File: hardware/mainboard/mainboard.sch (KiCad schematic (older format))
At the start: 7 parts, among them J1 2309407-1, J3 Conn_01x02_Male

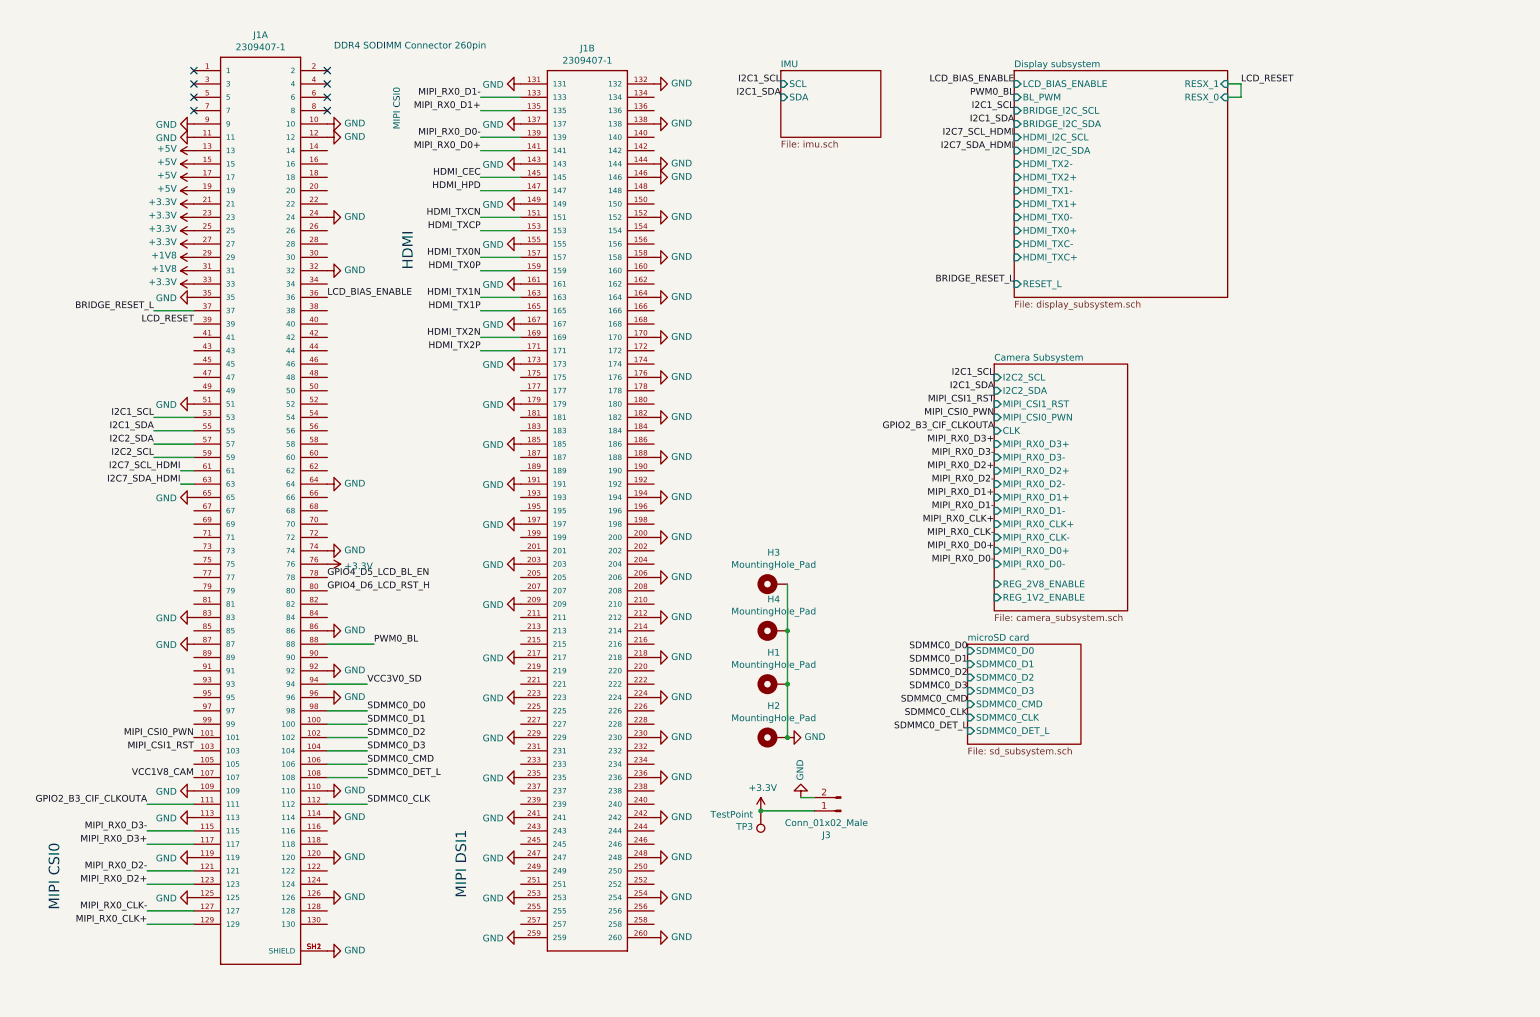
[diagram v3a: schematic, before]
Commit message: finish basic schematic, need to decide audio situation
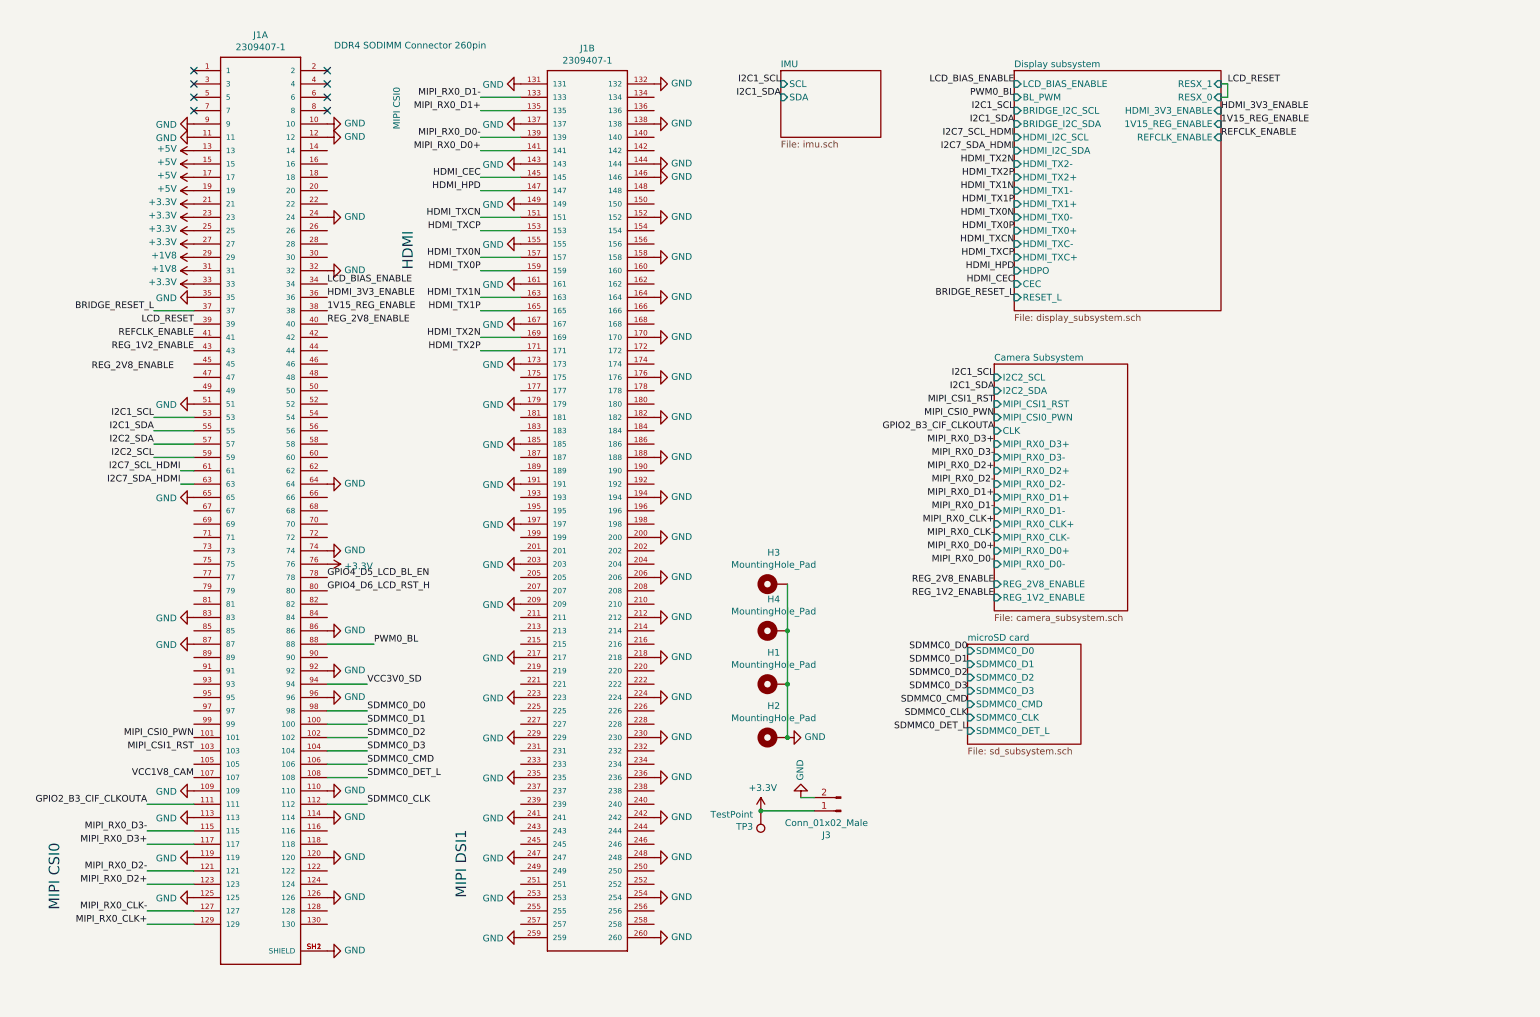
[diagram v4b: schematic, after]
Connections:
- net LCD_BIAS_ENABLE: now also J1.34; no longer J1.36
- net 1V15_REG_ENABLE: now reaches J1.38
- net REG_2V8_ENABLE: now reaches J1.40
- net REFCLK_ENABLE: now reaches J1.41
- net REG_1V2_ENABLE: now reaches J1.43
- new net HDMI_3V3_ENABLE: J1.36
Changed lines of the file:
@@
 F3 "SDA" I L 6150 1100 50
-$EndSheet
-$Sheet
-S 7900 900  1600 1700
-U 5FF71A49
-F0 "Display subsystem" 50
-F1 "display_subsystem.sch" 50
-F2 "LCD_BIAS_ENABLE" I L 7900 1000 50
-F3 "RESET_L" I L 7900 2500 50
-F4 "HDMI_TXC+" I L 7900 2300 50
-F5 "HDMI_TXC-" I L 7900 2200 50
-F6 "HDMI_TX0+" I L 7900 2100 50
-F7 "HDMI_TX0-" I L 7900 2000 50
-F8 "HDMI_TX1+" I L 7900 1900 50
-F9 "HDMI_TX1-" I L 7900 1800 50
-F10 "HDMI_TX2+" I L 7900 1700 50
-F11 "HDMI_TX2-" I L 7900 1600 50
-F12 "HDMI_I2C_SDA" I L 7900 1500 50
-F13 "HDMI_I2C_SCL" I L 7900 1400 50
-F14 "BRIDGE_I2C_SDA" I L 7900 1300 50
-F15 "BRIDGE_I2C_SCL" I L 7900 1200 50
-F16 "BL_PWM" I L 7900 1100 50
-F17 "RESX_1" I R 9500 1000 50
-F18 "RESX_0" I R 9500 1100 50
 $EndSheet
 Text Label 7750 3500 2    50   ~ 0
@@
 Text Label 7900 1000 2    50   ~ 0
 LCD_BIAS_ENABLE
-Text Label 2750 2600 0    50   ~ 0
+Text Label 2750 2500 0    50   ~ 0
 LCD_BIAS_ENABLE
 Text Label 7900 1100 2    50   ~ 0
@@
 Text Label 7900 1500 2    50   ~ 0
 I2C7_SDA_HDMI
-Text Label 7900 2500 2    50   ~ 0
+Text Label 7900 2600 2    50   ~ 0
 BRIDGE_RESET_L
 Text Label 1450 2700 2    50   ~ 0
@@
 Text Label 1750 2800 2    50   ~ 0
 LCD_RESET
-Text Label 9600 1000 0    50   ~ 0
+Text Label 9500 1000 0    50   ~ 0
 LCD_RESET
+$Sheet
+S 7900 900  1550 1800
+U 5FF71A49
+F0 "Display subsystem" 50
+F1 "display_subsystem.sch" 50
+F2 "LCD_BIAS_ENABLE" I L 7900 1000 50
+F3 "RESET_L" I L 7900 2600 50
+F4 "HDMI_TXC+" I L 7900 2300 50
+F5 "HDMI_TXC-" I L 7900 2200 50
+F6 "HDMI_TX0+" I L 7900 2100 50
+F7 "HDMI_TX0-" I L 7900 2000 50
+F8 "HDMI_TX1+" I L 7900 1900 50
+F9 "HDMI_TX1-" I L 7900 1800 50
+F10 "HDMI_TX2+" I L 7900 1700 50
+F11 "HDMI_TX2-" I L 7900 1600 50
+F12 "HDMI_I2C_SDA" I L 7900 1500 50
+F13 "HDMI_I2C_SCL" I L 7900 1400 50
+F14 "BRIDGE_I2C_SDA" I L 7900 1300 50
+F15 "BRIDGE_I2C_SCL" I L 7900 1200 50
+F16 "BL_PWM" I L 7900 1100 50
+F17 "RESX_1" I R 9450 1000 50
+F18 "RESX_0" I R 9450 1100 50
+F19 "CEC" I L 7900 2500 50
+F20 "HDPO" I L 7900 2400 50
+F21 "HDMI_3V3_ENABLE" I R 9450 1200 50
+F22 "1V15_REG_ENABLE" I R 9450 1300 50
+F23 "REFCLK_ENABLE" I R 9450 1400 50
+$EndSheet
+Text Label 7900 2300 2    50   ~ 0
+HDMI_TXCP
+Text Label 7900 2200 2    50   ~ 0
+HDMI_TXCN
+Text Label 7900 2100 2    50   ~ 0
+HDMI_TX0P
+Text Label 7900 2000 2    50   ~ 0
+HDMI_TX0N
+Text Label 7900 1900 2    50   ~ 0
+HDMI_TX1P
+Text Label 7900 1800 2    50   ~ 0
+HDMI_TX1N
+Text Label 7900 1700 2    50   ~ 0
+HDMI_TX2P
+Text Label 7900 1600 2    50   ~ 0
+HDMI_TX2N
 Wire Wire Line
-	9500 1000 9600 1000
+	9450 1000 9500 1000
 Wire Wire Line
-	9500 1100 9600 1100
+	9500 1000 9500 1100
 Wire Wire Line
-	9600 1100 9600 1000
+	9500 1100 9450 1100
+Text Label 7900 2400 2    50   ~ 0
+HDMI_HPD
+Text Label 7900 2500 2    50   ~ 0
+HDMI_CEC
+Text Label 9450 1200 0    50   ~ 0
+HDMI_3V3_ENABLE
+Text Label 9450 1300 0    50   ~ 0
+1V15_REG_ENABLE
+Text Label 9450 1400 0    50   ~ 0
+REFCLK_ENABLE
+Text Label 2750 2600 0    50   ~ 0
+HDMI_3V3_ENABLE
+Text Label 1750 2900 2    50   ~ 0
+REFCLK_ENABLE
+Text Label 2750 2700 0    50   ~ 0
+1V15_REG_ENABLE
+Text Label 7750 4850 2    50   ~ 0
+REG_1V2_ENABLE
+Text Label 1750 3000 2    50   ~ 0
+REG_1V2_ENABLE
+Text Label 7750 4750 2    50   ~ 0
+REG_2V8_ENABLE
+Text Label 1600 3150 2    50   ~ 0
+REG_2V8_ENABLE
+Text Label 2750 2800 0    50   ~ 0
+REG_2V8_ENABLE
 $EndSCHEMATC

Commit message: cleanup, audio pll, decide board layout
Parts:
- added FID? (x5): Fiducial, symbol Mechanical:Fiducial
- added J?: Conn_01x02_Male, Connector_PinHeader_2.54mm:PinHeader_1x02_P2.54mm_Vertical, symbol Connector:Conn_01x02_Male
- added TP? (x2): TestPoint, symbol Connector:TestPoint
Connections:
- net I2C1_SCL: now also TP?.1
- net I2C1_SDA: now also TP?.1
- net 1V8_REG_ENABLE: now reaches J1.42
- net UART2DBG_TX: now reaches J1.52
- net UART2DBG_TX: now also J?.1 (Pin_1)
- net UART2DBG_RX: now reaches J1.54
- net UART2DBG_RX: now also J?.2 (Pin_2)
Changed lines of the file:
@@
 $Descr A4 11693 8268
 encoding utf-8
-Sheet 1 7
+Sheet 1 8
 Title ""
 Date ""
@@
 Wire Wire Line
 	1450 3800 1750 3800
-Text Label 6150 1000 2    50   ~ 0
+Text Label 6000 1000 2    50   ~ 0
 I2C1_SCL
-Text Label 6150 1100 2    50   ~ 0
+Text Label 6000 1100 2    50   ~ 0
 I2C1_SDA
 $Comp
@@
 F0 "microSD card" 50
 F1 "sd_subsystem.sch" 50
-F2 "SDMMC0_D2" I L 7550 5450 50
-F3 "SDMMC0_D3" I L 7550 5550 50
-F4 "SDMMC0_CMD" I L 7550 5650 50
-F5 "SDMMC0_CLK" I L 7550 5750 50
-F6 "SDMMC0_D0" I L 7550 5250 50
-F7 "SDMMC0_D1" I L 7550 5350 50
-F8 "SDMMC0_DET_L" I L 7550 5850 50
+F2 "SDMMC0_D2" I L 7550 5700 50
+F3 "SDMMC0_D3" I L 7550 5600 50
+F4 "SDMMC0_CMD" I L 7550 5500 50
+F5 "SDMMC0_CLK" I L 7550 5400 50
+F6 "SDMMC0_D0" I L 7550 5900 50
+F7 "SDMMC0_D1" I L 7550 5800 50
+F8 "SDMMC0_DET_L" I L 7550 5300 50
 $EndSheet
-Text Label 7550 5250 2    50   ~ 0
+Text Label 7550 5900 2    50   ~ 0
 SDMMC0_D0
-Text Label 7550 5350 2    50   ~ 0
+Text Label 7550 5800 2    50   ~ 0
 SDMMC0_D1
-Text Label 7550 5550 2    50   ~ 0
+Text Label 7550 5600 2    50   ~ 0
 SDMMC0_D3
-Text Label 7550 5650 2    50   ~ 0
+Text Label 7550 5500 2    50   ~ 0
 SDMMC0_CMD
-Text Label 7550 5850 2    50   ~ 0
+Text Label 7550 5300 2    50   ~ 0
 SDMMC0_DET_L
-Text Label 7550 5750 2    50   ~ 0
+Text Label 7550 5400 2    50   ~ 0
 SDMMC0_CLK
-Text Label 7550 5450 2    50   ~ 0
+Text Label 7550 5700 2    50   ~ 0
 SDMMC0_D2
 Text Label 7750 3200 2    50   ~ 0
@@
 F22 "1V15_REG_ENABLE" I R 9450 1300 50
 F23 "REFCLK_ENABLE" I R 9450 1400 50
+F24 "BRIDGE_1V8_REG_ENABLE" I R 9450 1600 50
 $EndSheet
 Text Label 7900 2300 2    50   ~ 0
@@
 Text Label 7750 4750 2    50   ~ 0
 REG_2V8_ENABLE
-Text Label 1600 3150 2    50   ~ 0
-REG_2V8_ENABLE
 Text Label 2750 2800 0    50   ~ 0
 REG_2V8_ENABLE
+$Comp
+L Mechanical:Fiducial FID?
+U 1 1 5FEFD4AC
+P 6050 3150
+F 0 "FID?" H 6135 3196 50  0000 L CNN
+F 1 "Fiducial" H 6135 3105 50  0000 L CNN
+F 2 "" H 6050 3150 50  0001 C CNN
+F 3 "~" H 6050 3150 50  0001 C CNN
+	1    6050 3150
+	1    0    0    -1
+$EndComp
+$Comp
+L Mechanical:Fiducial FID?
+U 1 1 5FEFDC53
+P 6050 3450
+F 0 "FID?" H 6135 3496 50  0000 L CNN
+F 1 "Fiducial" H 6135 3405 50  0000 L CNN
+F 2 "" H 6050 3450 50  0001 C CNN
+F 3 "~" H 6050 3450 50  0001 C CNN
+	1    6050 3450
+	1    0    0    -1
+$EndComp
+$Comp
+L Mechanical:Fiducial FID?
+U 1 1 5FEFEBAF
+P 6050 3750
+F 0 "FID?" H 6135 3796 50  0000 L CNN
+F 1 "Fiducial" H 6135 3705 50  0000 L CNN
+F 2 "" H 6050 3750 50  0001 C CNN
+F 3 "~" H 6050 3750 50  0001 C CNN
+	1    6050 3750
+	1    0    0    -1
+$EndComp
+$Comp
+L Mechanical:Fiducial FID?
+U 1 1 5FEFFA9D
+P 6050 4050
+F 0 "FID?" H 6135 4096 50  0000 L CNN
+F 1 "Fiducial" H 6135 4005 50  0000 L CNN
+F 2 "" H 6050 4050 50  0001 C CNN
+F 3 "~" H 6050 4050 50  0001 C CNN
+	1    6050 4050
+	1    0    0    -1
+$EndComp
+$Comp
+L Mechanical:Fiducial FID?
+U 1 1 5FF00982
+P 6050 4350
+F 0 "FID?" H 6135 4396 50  0000 L CNN
+F 1 "Fiducial" H 6135 4305 50  0000 L CNN
+F 2 "" H 6050 4350 50  0001 C CNN
+F 3 "~" H 6050 4350 50  0001 C CNN
+	1    6050 4350
+	1    0    0    -1
+$EndComp
+Wire Wire Line
+	6000 1000 6150 1000
+Wire Wire Line
+	6000 1100 6150 1100
+$Comp
+L Connector:TestPoint TP?
+U 1 1 5FF30886
+P 6000 1100
+AR Path="/5FF71A49/5FF30886" Ref="TP?"  Part="1"
+AR Path="/5FF30886" Ref="TP?"  Part="1"
+F 0 "TP?" V 5954 1288 50  0001 L CNN
+F 1 "TestPoint" V 6045 1288 50  0001 L CNN
+F 2 "" H 6200 1100 50  0001 C CNN
+F 3 "~" H 6200 1100 50  0001 C CNN
+	1    6000 1100
+	-1   0    0    1
+$EndComp
+$Comp
+L Connector:TestPoint TP?
+U 1 1 5FF31F81
+P 6000 1000
+AR Path="/5FF71A49/5FF31F81" Ref="TP?"  Part="1"
+AR Path="/5FF31F81" Ref="TP?"  Part="1"
+F 0 "TP?" V 5954 1188 50  0001 L CNN
+F 1 "TestPoint" V 6045 1188 50  0001 L CNN
+F 2 "" H 6200 1000 50  0001 C CNN
+F 3 "~" H 6200 1000 50  0001 C CNN
+	1    6000 1000
+	1    0    0    -1
+$EndComp
+Text Label 9450 1600 0    50   ~ 0
+1V8_REG_ENABLE
+Text Label 2750 2900 0    50   ~ 0
+1V8_REG_ENABLE
+Text Label 2750 3400 0    50   ~ 0
+UART2DBG_TX
+Text Label 2750 3500 0    50   ~ 0
+UART2DBG_RX
+Text Label 6450 6950 2    50   ~ 0
+UART2DBG_TX
+Text Label 6450 6850 2    50   ~ 0
+UART2DBG_RX
+$Comp
+L Connector:Conn_01x02_Male J?
+U 1 1 6002C20F
+P 6650 6950
+F 0 "J?" H 6758 7131 50  0000 C CNN
+F 1 "Conn_01x02_Male" H 6758 7040 50  0000 C CNN
+F 2 "Connector_PinHeader_2.54mm:PinHeader_1x02_P2.54mm_Vertical" H 6650 6950 50  0001 C CNN
+F 3 "~" H 6650 6950 50  0001 C CNN
+	1    6650 6950
+	-1   0    0    1
+$EndComp
+$Sheet
+S 9400 3100 850  900
+U 60213121
+F0 "Audio subsystem" 50
+F1 "audio.sch" 50
+$EndSheet
 $EndSCHEMATC
